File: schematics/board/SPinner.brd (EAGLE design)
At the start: 63.6 x 63.6 mm, 8 parts

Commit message: Платы СБ
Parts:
- added U$5: KCONNECTQUAD, CanCubeSat:KCONNECT_QUAD
- moved U$4 8.30 mm to (54.4, 54.4)
- moved U$3 8.29 mm to (62.9, 62.9)
- moved U$2 5.89 mm to (15.6, 54.4)
- moved U$21 5.89 mm to (54.4, 15.6)
- moved U$1 5.88 mm to (7.07, 62.9)
- moved U$20 5.88 mm to (62.9, 7.07)
- moved U$19 0.72 mm to (15.6, 15.6)
- moved U$18 0.71 mm to (7.07, 7.07)
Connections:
- new net CMD: U$5.1, U$5.2, U$5.3, U$5.4, U$5.P$1, U$5.P$2
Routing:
- net BUS+1: track 75.4 -> 0.00 mm
- net CMD: track 0.00 -> 18.4 mm
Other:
- board size 63.6 x 63.6 mm -> 70 x 70 mm

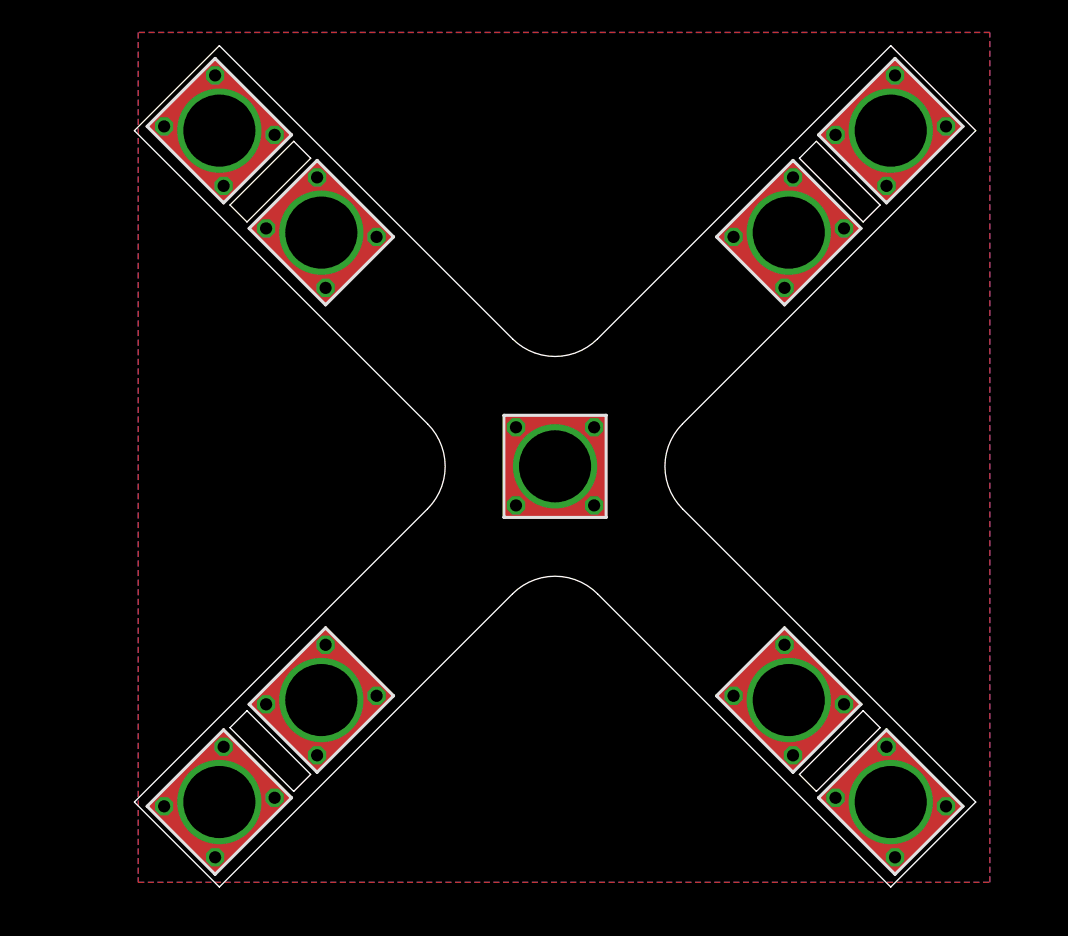
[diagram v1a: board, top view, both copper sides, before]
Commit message: Добавлена схема дозиметра, исправлены платы СБ
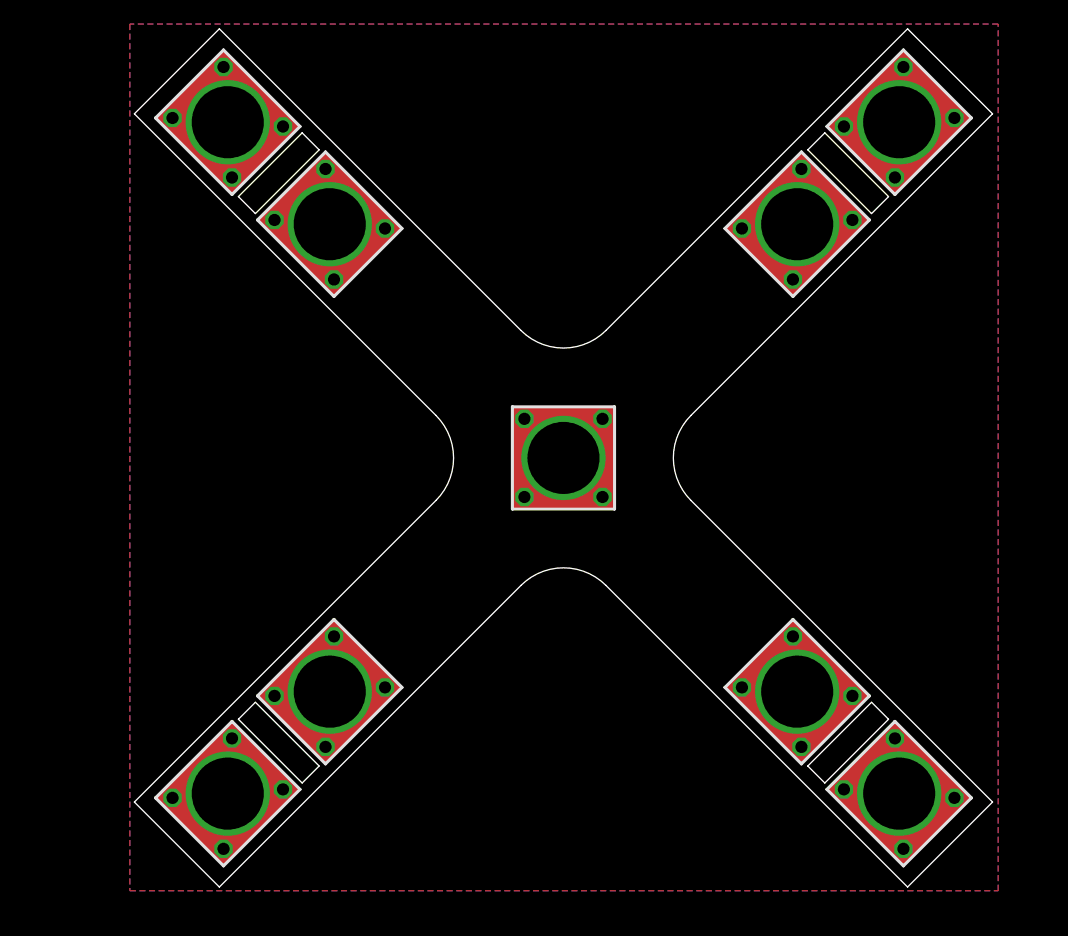
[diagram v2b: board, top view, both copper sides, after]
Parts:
- moved U$3 0.99 mm to (63.6, 63.6)
- moved U$1 0.99 mm to (7.77, 63.6)
- moved U$20 0.99 mm to (63.6, 7.77)
- moved U$19 0.99 mm to (16.3, 16.3)
- moved U$18 0.99 mm to (7.77, 7.77)
- moved U$2 0.99 mm to (16.3, 55.1)
- moved U$21 0.99 mm to (55.1, 16.3)
- moved U$4 0.99 mm to (55.1, 55.1)
- moved U$5 0.99 mm to (35.7, 35.7)
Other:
- board size 70 x 70 mm -> 71.4 x 71.4 mm
